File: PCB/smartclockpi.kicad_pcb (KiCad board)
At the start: 2 copper layers, 17 parts, among them J1 Raspberry_Pi_2_3, J2 DS3231 RTC module, J3 ILI9488 SPI TFT touchscreen, J4 PCM5102A DAC (with headphone 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, U1 BME280, U2 MCP3008

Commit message: finallise pcb. spent toooo much time on this...
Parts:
- removed R10, R11: 4.7kΩ, Resistor_THT:R_Axial_DIN0204_L3.6mm_D1.6mm_P5.08mm_Vertical
- removed U1: BME280, Connector_PinSocket_2.54mm:PinSocket_1x06_P2.54mm_Vertical
- added R12: 4.7kΩ, Resistor_THT:R_Axial_DIN0204_L3.6mm_D1.6mm_P5.08mm_Vertical, F.Cu at (110.2, 83.1)
- added R13: 4.7kΩ, Resistor_THT:R_Axial_DIN0204_L3.6mm_D1.6mm_P5.08mm_Vertical, F.Cu at (110.2, 86.2)
- added U3: DHT22, Sensor:Aosong_DHT11_5.5x12.0_P2.54mm, F.Cu at (99.8, 79.9)
- J2: footprint Connector_PinSocket_2.54mm:PinSocket_1x07_P2.54mm_Vertical -> Connector_PinSocket_2.54mm:PinSocket_1x06_P2.54mm_Horizontal
- moved J2 15.6 mm to (117.1, 133.0), turned to -90 degrees
- moved J3 0.60 mm to (62.5, 88.7)
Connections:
- J1 pad 26: unconnected-(J1-~{CE1}/GPIO7-Pad26) -> Net-(J1-~{CE1}/GPIO7)
- J2 pad 1: (no net) -> Net-(J2-32K)
- J2 pad 2: (no net) -> Net-(J2-SQW)
- J2 pad 3: (no net) -> Net-(J1-SCL/GPIO3)
- J2 pad 4: (no net) -> Net-(J1-SDA/GPIO2)
- J2 pad 5: (no net) -> +3.3V
- J2 pad 6: (no net) -> GND
- J3 pad 1: (no net) -> +3.3V
- J3 pad 10: (no net) -> Net-(J1-GCLK2/GPIO6)
- J3 pad 11: (no net) -> Net-(J1-GCLK1/GPIO5)
- J3 pad 12: (no net) -> Net-(J1-PWM0/GPIO12)
- J3 pad 13: (no net) -> Net-(J1-GPIO23)
- J3 pad 14: (no net) -> Net-(J1-GPIO16)
- J3 pad 2: (no net) -> GND
- J3 pad 3: (no net) -> Net-(J1-~{CE0}/GPIO8)
- J3 pad 4: (no net) -> Net-(J1-GPIO25)
- J3 pad 5: (no net) -> Net-(J1-GPIO24)
- J3 pad 6: (no net) -> Net-(J1-MOSI0/GPIO10)
- J3 pad 7: (no net) -> Net-(J1-SCLK0/GPIO11)
- J3 pad 8: (no net) -> Net-(J1-PWM1/GPIO13)
- J3 pad 9: (no net) -> Net-(J1-MISO0/GPIO9)
- J4 pad 1: (no net) -> unconnected-(J4-SCK-Pad1)
- J4 pad 2: (no net) -> Net-(J1-GPIO18/PWM0)
- J4 pad 3: (no net) -> Net-(J1-GPIO21/SCLK1)
- J4 pad 4: (no net) -> Net-(J1-GPIO19/MISO1)
- J4 pad 5: (no net) -> GND
- J4 pad 6: (no net) -> +5V
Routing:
- net +3.3V: track 0.00 -> 181.2 mm, vias 0 -> 1
- net Net-(J1-MOSI0/GPIO10): track 0.00 -> 154.4 mm
- net Net-(J1-SDA/GPIO2): track 0.00 -> 122.2 mm
- net Net-(J1-SCL/GPIO3): track 0.00 -> 121.3 mm
- net Net-(J1-GPIO19/MISO1): track 0.00 -> 108.9 mm, vias 0 -> 3
- net Net-(J1-GCLK0/GPIO4): track 0.00 -> 104.7 mm
- net Net-(J1-~{CE1}/GPIO7): track 0.00 -> 70.3 mm
- net GND: track 0.00 -> 63.9 mm, vias 0 -> 1
- net Net-(J1-MISO0/GPIO9): track 0.00 -> 63.8 mm
- net Net-(J1-GPIO21/SCLK1): track 0.00 -> 63.3 mm, vias 0 -> 1
- net Net-(J1-SCLK0/GPIO11): track 0.00 -> 61.0 mm
- net Net-(J2-SQW): track 0.00 -> 55.4 mm
- net Net-(J2-32K): track 0.00 -> 53.6 mm
- net Net-(U2-CH0): track 0.00 -> 47.9 mm
- net +5V: track 0.00 -> 41.8 mm
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- added copper zone on B.Cu, net GND
- added copper zone on F.Cu, net GND
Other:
- board outline added: 83 x 71 mm

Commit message: update pcb
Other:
- board text added: "Copyleft 2025 Raymont Qin (QinCai) Some rights reserved Licensed under the GPLv3 License github.com/QinCai-rui/SmartClockPi"
- board text added: "Rev. 1.0"
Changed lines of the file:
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@@
 		(layer "Edge.Cuts")
+	)
+	(gr_text "Rev. 1.0"
+		(at 112.75 72.25 0)
+		(layer "F.SilkS")
+		(effects
+			(font
+				(size 1 1)
+				(thickness 0.2)
+				(bold yes)
+			)
+			(justify left bottom)
+		)
+	)
+	(gr_text "Copyleft 2025 Raymont Qin (QinCai)\nSome rights reserved\nLicensed under the GPLv3 License\n\ngithub.com/QinCai-rui/SmartClockPi"
+		(at 48 77.25 0)
+		(layer "F.SilkS")
+		(effects
+			(font
+				(size 1 1)
+				(thickness 0.125)
+			)
+			(justify left bottom)
+		)
 	)
 	(segment

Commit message: update pcb. idk what i did
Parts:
- J1: value Raspberry_Pi_2_3 -> Raspberry_Pi
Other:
- board size 83 x 71 mm -> 80.7 x 67.1 mm
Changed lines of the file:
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@@
 			)
 		)
-		(property "Value" "Raspberry_Pi_2_3"
+		(property "Value" "Raspberry_Pi"
 			(at -1.27 51.03 0)
 			(layer "F.Fab")
@@
 	)
 	(gr_rect
-		(start 38.5 66)
-		(end 121.5 137)
+		(start 40 69)
+		(end 120.6886 136.1138)
 		(stroke
 			(width 0.05)

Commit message: add in usb ports
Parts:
- added J5: USB_B_Micro, Connector_USB:USB_Micro-B_Amphenol_10118193-0001LF_Horizontal, F.Cu at (111.2, 70.9)
- added J6: USB_A, Connector_USB:USB_A_Receptacle_GCT_USB1046, F.Cu at (126.1, 75.0)
- added J7: microUSB IN, Connector_PinSocket_2.54mm:PinSocket_1x02_P2.54mm_Vertical, F.Cu at (121.7, 90.4)
- added J8: USB-A OUT, Connector_PinSocket_2.54mm:PinSocket_1x02_P2.54mm_Vertical, F.Cu at (129.6, 90.4)
- added J9: PWR IN, Connector_PinSocket_2.54mm:PinSocket_1x02_P2.54mm_Vertical, F.Cu at (89.5, 84.9)
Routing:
- net Net-(J5-VBUS): track 0.00 -> 21.0 mm
- net Net-(J6-VBUS): track 0.00 -> 8.21 mm
- net +5V: track 41.8 -> 48.8 mm
- net GND: track 63.9 -> 64.5 mm
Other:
- board size 80.7 x 67.1 mm -> 94.5 x 67.1 mm
- board text added: "+"
- board text added: "-"

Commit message: update PCB
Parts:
- added D1: 1N4001, Diode_THT:D_DO-41_SOD81_P10.16mm_Horizontal, F.Cu at (73.8, 90.8)
- J4: value PCM5102A DAC (with headphone jack) -> PCM5102A DAC
- moved J2 4.12 mm to (121.1, 132.0)
- moved J5 2.06 mm to (109.1, 70.9)
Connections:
- J9 pad 1: +5V -> Net-(D1-A)
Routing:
- net GND: track 64.5 -> 43.8 mm
- net Net-(D1-A): track 0.00 -> 8.31 mm
- net Net-(J2-SQW): track 55.4 -> 49.3 mm
- net +3.3V: track 181.2 -> 175.5 mm, vias 1 -> 2
- net +5V: track 48.8 -> 54.2 mm
- net Net-(J1-SDA/GPIO2): track 122.2 -> 119.3 mm
- net Net-(J5-VBUS): track 21.0 -> 21.8 mm
- net Net-(J1-SCL/GPIO3): track 121.3 -> 122.0 mm
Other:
- board text added: "Rev. 1.1"
- board text removed: "Rev. 1.0"

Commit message: update pcb and stuff
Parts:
- removed J4: PCM5102A DAC, Connector_PinSocket_2.54mm:PinSocket_1x06_P2.54mm_Vertical
- J1: footprint Connector_PinSocket_2.54mm:PinSocket_2x20_P2.54mm_Vertical -> Connector_PinHeader_2.54mm:PinHeader_2x20_P2.54mm_Vertical
- moved J1 2.57 mm to (44.5, 81.8)
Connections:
- J1 pad 11: unconnected-(J1-GPIO17-Pad11) -> Net-(J1-GPIO17)
- J1 pad 12: Net-(J1-GPIO18/PWM0) -> unconnected-(J1-GPIO18/PWM0-Pad12)
- J1 pad 16: Net-(J1-GPIO23) -> unconnected-(J1-GPIO23-Pad16)
- J1 pad 29: Net-(J1-GCLK1/GPIO5) -> unconnected-(J1-GCLK1/GPIO5-Pad29)
- J1 pad 31: Net-(J1-GCLK2/GPIO6) -> unconnected-(J1-GCLK2/GPIO6-Pad31)
- J1 pad 36: Net-(J1-GPIO16) -> unconnected-(J1-GPIO16-Pad36)
- J1 pad 38: unconnected-(J1-GPIO20/MOSI1-Pad38) -> Net-(J1-GPIO20/MOSI1)
- J3 pad 10: Net-(J1-GCLK2/GPIO6) -> Net-(J1-GPIO21/SCLK1)
- J3 pad 11: Net-(J1-GCLK1/GPIO5) -> Net-(J1-GPIO20/MOSI1)
- J3 pad 12: Net-(J1-PWM0/GPIO12) -> Net-(J1-GPIO19/MISO1)
- J3 pad 13: Net-(J1-GPIO23) -> Net-(J1-GPIO17)
- J3 pad 14: Net-(J1-GPIO16) -> Net-(J1-PWM0/GPIO12)
- U2 pad 10: Net-(J1-GCLK0/GPIO4) -> Net-(J1-~{CE1}/GPIO7)
- U3 pad 2: Net-(J1-~{CE1}/GPIO7) -> Net-(J1-GCLK0/GPIO4)
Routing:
- net Net-(J1-GPIO19/MISO1): track 108.9 -> 22.5 mm, vias 3 -> 2
- net Net-(J1-MOSI0/GPIO10): track 154.4 -> 102.3 mm
- net Net-(J1-GPIO17): track 0.00 -> 39.5 mm, vias 0 -> 3
- net Net-(J1-GPIO23): track 38.2 -> 0.00 mm, vias 1 -> 0
- net Net-(J1-GPIO20/MOSI1): track 0.00 -> 37.0 mm
- net Net-(J1-GPIO18/PWM0): track 33.1 -> 0.00 mm, vias 1 -> 0
- net Net-(J1-GCLK0/GPIO4): track 104.7 -> 75.1 mm, vias 0 -> 1
- net Net-(J1-GCLK1/GPIO5): track 24.6 -> 0.00 mm, vias 1 -> 0
- net +5V: track 54.2 -> 32.0 mm
- net Net-(J1-GPIO16): track 20.5 -> 0.00 mm
- net Net-(J1-GCLK2/GPIO6): track 19.5 -> 0.00 mm, vias 1 -> 0
- net GND: track 43.8 -> 26.1 mm, vias 1 -> 0
- net Net-(J1-GPIO24): track 33.3 -> 16.8 mm
- net Net-(J1-GPIO21/SCLK1): track 63.3 -> 51.9 mm, vias 1 -> 0
- net Net-(J1-GPIO25): track 29.9 -> 20.0 mm
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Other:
- board text added: "Rev. 1.2"
- board text removed: "Rev. 1.1"

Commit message: modify pcb
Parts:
- added REF**: MountingHole_2.2mm_M2, MountingHole:MountingHole_2.2mm_M2, F.Cu at (53.0, 119.0)
- added REF**: MountingHole_2.2mm_M2, MountingHole:MountingHole_2.2mm_M2, F.Cu at (81.0, 128.5)
- added REF**: MountingHole_2.2mm_M2, MountingHole:MountingHole_2.2mm_M2, F.Cu at (115.7, 72.5)
- added REF**: MountingHole_2.2mm_M2, MountingHole:MountingHole_2.2mm_M2, F.Cu at (43.5, 73.0)
- added REF**: MountingHole_2.2mm_M2, MountingHole:MountingHole_2.2mm_M2, F.Cu at (82.0, 72.5)
- added REF**: MountingHole_2.2mm_M2, MountingHole:MountingHole_2.2mm_M2, F.Cu at (130.0, 102.5)
- added REF**: MountingHole_2.2mm_M2, MountingHole:MountingHole_2.2mm_M2, F.Cu at (130.0, 131.5)
- moved J5 0.79 mm to (108.3, 70.9)

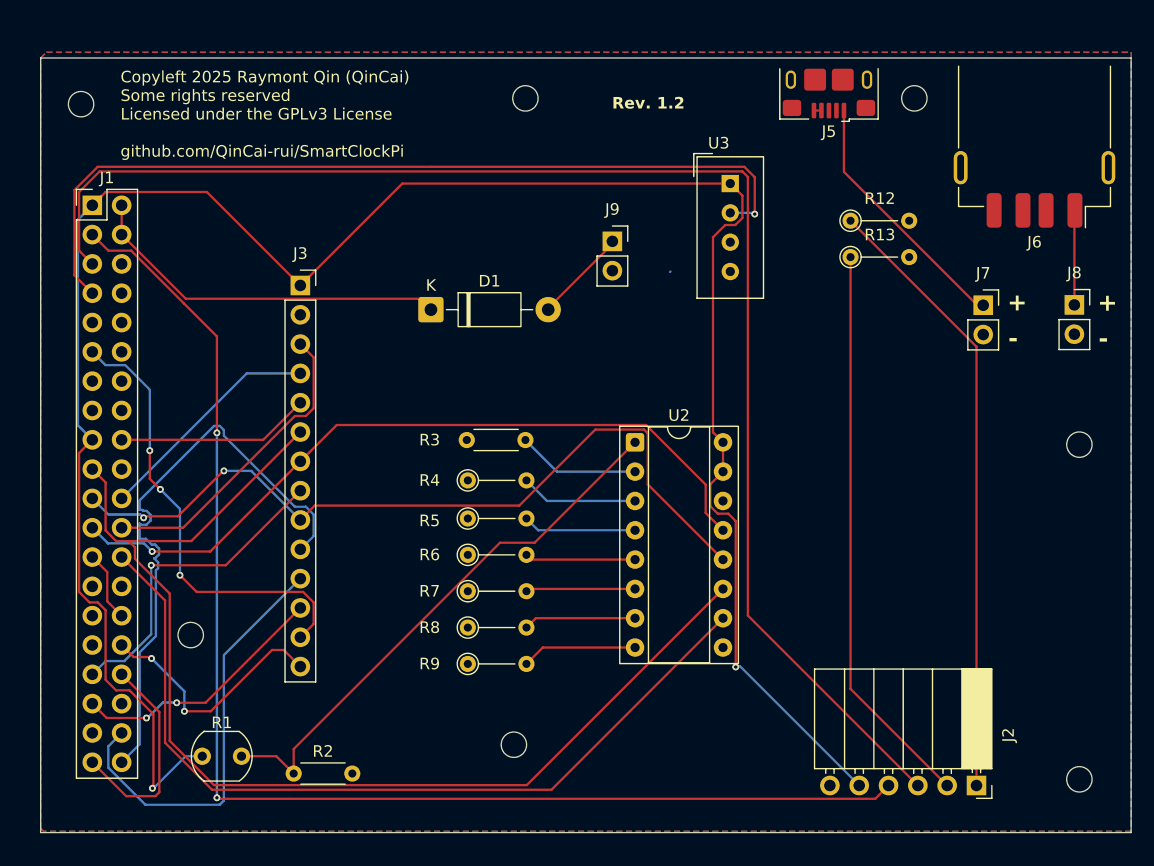
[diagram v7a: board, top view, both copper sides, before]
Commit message: fix resistor positions
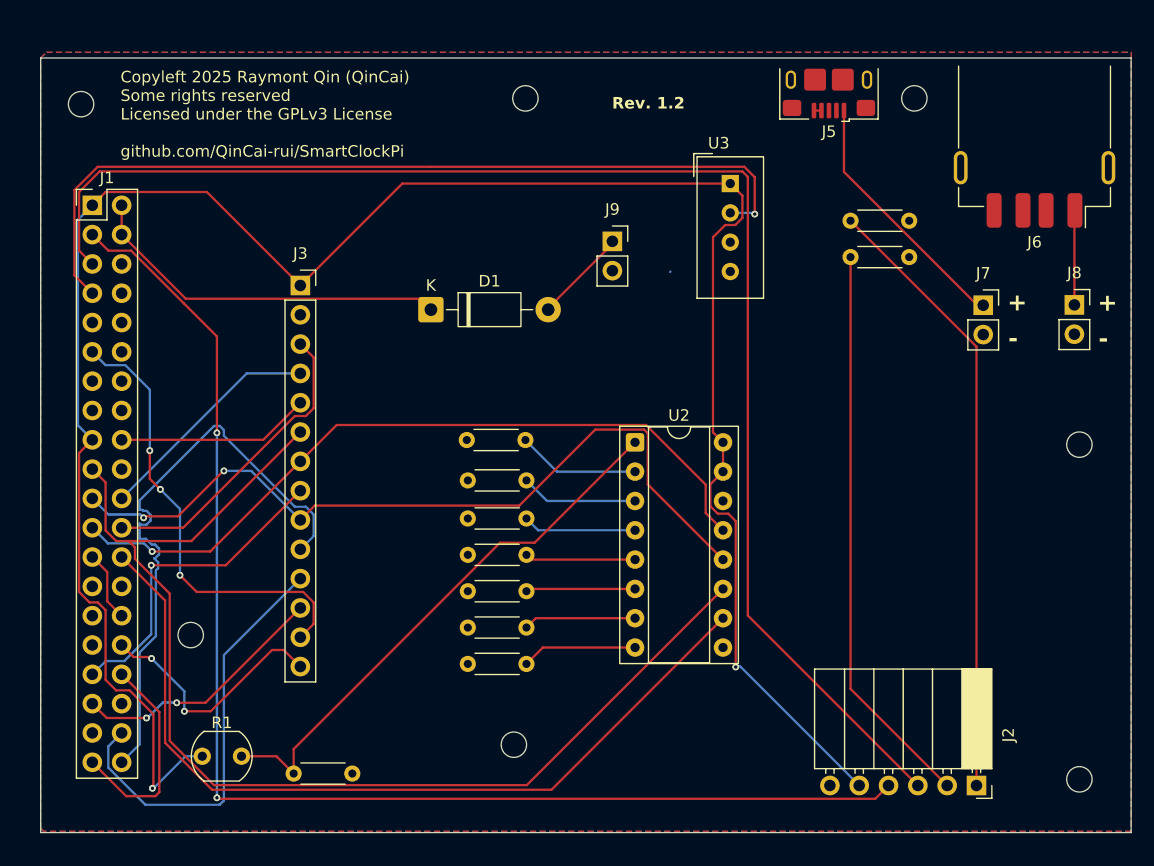
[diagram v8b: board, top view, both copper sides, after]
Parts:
- R12, R13, R4, R5, R6, R7, R8, R9: footprint Resistor_THT:R_Axial_DIN0204_L3.6mm_D1.6mm_P5.08mm_Vertical -> Resistor_THT:R_Axial_DIN0204_L3.6mm_D1.6mm_P5.08mm_Horizontal
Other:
- board text added: "R3"
